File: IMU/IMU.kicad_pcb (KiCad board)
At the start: 2 copper layers, 14 parts, among them IC1 ADXL326BCPZ-RL7, U1 DEV-16771, U2 IAM-20380, U3 MLX90393SLW-ABA-011-RE

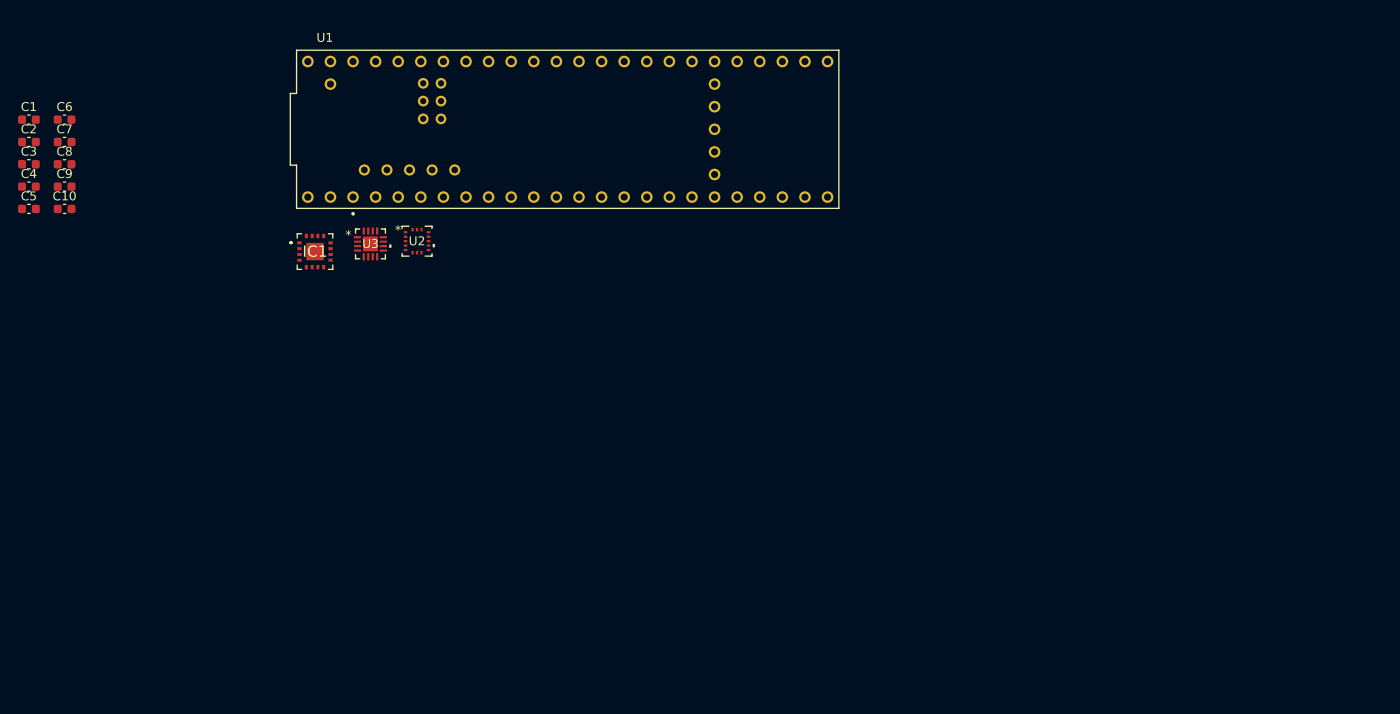
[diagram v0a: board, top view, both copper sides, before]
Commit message: Some layout changes
Added filled zomes, linked 3d models, added board edge cuts and mounting holes (still need to add filled zone exclusions around the mounting holes to prevent shorts, though I will probably just reduced the filled zomes anyways. Also should probably change which analog pins get used for the Gyro before routing traces/vias.
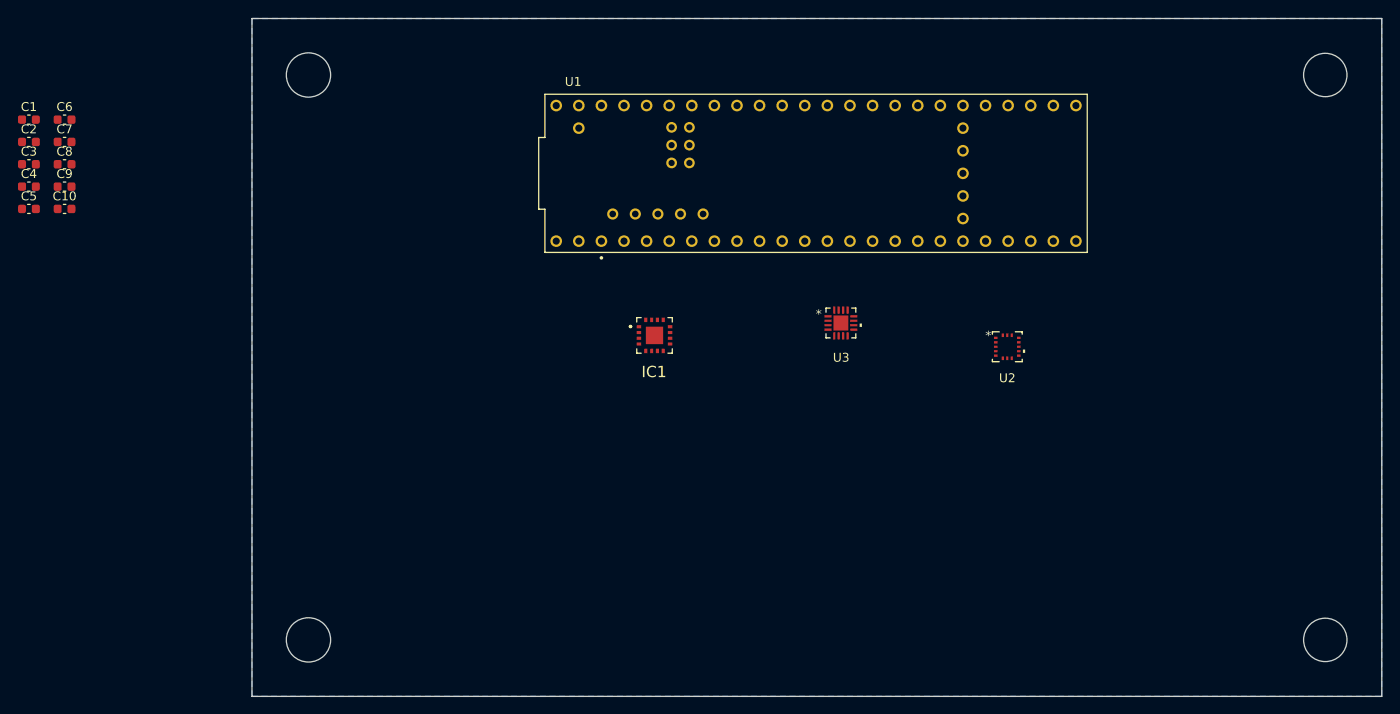
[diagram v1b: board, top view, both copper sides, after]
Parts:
- moved U2 67.4 mm to (172.0, 101.4)
- moved U3 53.6 mm to (153.3, 98.7)
- moved IC1 39.3 mm to (132.3, 100.1)
- moved U1 28.4 mm to (150.5, 81.9)
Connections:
- U1 pad GND1: unconnected-(U1-GND-PadGND1) -> /GND
- U1 pad GND2: unconnected-(U1-GND__1-PadGND2) -> /GND
- U1 pad GND3: unconnected-(U1-GND__2-PadGND3) -> /GND
- U1 pad GND4: unconnected-(U1-GND__3-PadGND4) -> /GND
- U1 pad GND5: unconnected-(U1-GND__4-PadGND5) -> /GND
- U1 pad USB_GND1: unconnected-(U1-USB_GND-PadUSB_GND1) -> /GND
- U1 pad USB_GND2: unconnected-(U1-USB_GND__1-PadUSB_GND2) -> /GND
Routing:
- added copper zone on In2.Cu, net /3P3V
- added copper zone on B.Cu, net /GND
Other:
- board outline added: 127 x 76.2 mm
- copper layers 2 -> 4

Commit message: Some minor Layout changes
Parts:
- added R1: 0, Resistor_SMD:R_0603_1608Metric, F.Cu at (143.0, 73.3)
- added R10: 0, Resistor_SMD:R_0603_1608Metric, F.Cu at (125.2, 100.5)
- added R11: 0, Resistor_SMD:R_0603_1608Metric, F.Cu at (145.5, 73.3)
- added R2: 0, Resistor_SMD:R_0603_1608Metric, F.Cu at (150.6, 100.8)
- added R3: 0, Resistor_SMD:R_0603_1608Metric, F.Cu at (155.6, 73.3)
- added R4: 0, Resistor_SMD:R_0603_1608Metric, F.Cu at (153.1, 100.8)
- added R5: 0, Resistor_SMD:R_0603_1608Metric, F.Cu at (155.7, 100.7)
- added R6: 0, Resistor_SMD:R_0603_1608Metric, F.Cu at (140.5, 73.3)
- added R7: 0, Resistor_SMD:R_0603_1608Metric, F.Cu at (168.5, 100.7)
- added R8: 0, Resistor_SMD:R_0603_1608Metric, F.Cu at (165.8, 100.7)
- added R9: 0, Resistor_SMD:R_0603_1608Metric, F.Cu at (127.8, 100.5)
- added TP1: TestPoint, TestPoint:TestPoint_Pad_4.0x4.0mm, F.Cu at (71.5, 107.7)
- added TP2: TestPoint, TestPoint:TestPoint_Pad_4.0x4.0mm, F.Cu at (71.5, 113.8)
- moved C5 75.9 mm to (133.2, 112.1)
- moved C6 72.3 mm to (130.3, 109.0)
- moved U2 35.7 mm to (136.8, 107.1)
- moved U3 19.6 mm to (171.4, 106.2)
- moved IC1 18.4 mm to (148.8, 108.2)
- moved U1 5.28 mm to (151.9, 87.0)
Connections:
- U2 pad 2: /SCK_Gyro -> Net-(U2-SCL/SPC)
- U2 pad 3: /MOSI_Gyro -> Net-(U2-SDA/SDI)
- U2 pad 4: /MISO_Gyro -> Net-(U2-SA0/SDO)
- U2 pad 5: /CS_Gyro -> Net-(U2-CS)
- U2 pad 6: /INT_Gyro -> Net-(U2-INT)
- U3 pad 1: /INT_Mag -> Net-(U3-INT)
- U3 pad 2: /CS_Mag -> Net-(U3-SENB/CS)
- U3 pad 3: /SCK_Mag -> Net-(U3-SCL/SCLK)
- U3 pad 5: /MOSI_Mag -> Net-(U3-SDA/MOSI)
- U3 pad 6: /MISO_Mag -> Net-(U3-MISO)
- U3 pad 7: /TRIG_Mag -> Net-(U3-INT/TRIG)

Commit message: m
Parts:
- removed C1, C2, C3: 3 nF, Capacitor_SMD:C_0603_1608Metric
- removed C4: 0.01 uF, Capacitor_SMD:C_0603_1608Metric
- removed IC1: ADXL326BCPZ-RL7, ADXL326BCPZ-RL7:ADXL326BCPZRL7
- removed R1, R10, R11, R2, R3, R4, R5, R6, R7, R8, R9: 0, Resistor_SMD:R_0603_1608Metric
- removed TP1, TP2: TestPoint, TestPoint:TestPoint_Pad_4.0x4.0mm
- removed U1: DEV-16771, DEV-16771:DEV-16771
- added U4: RASPBERRY_PI_PICO, Raspberry Pi:RASPBERRY_PI_PICO, F.Cu at (151.4, 81.0)
- added U5: ADXL380-1BCCZ-RL7, ADXL380:ADXL380, F.Cu at (132.8, 103.7)
- moved C8 108.6 mm to (169.2, 115.0)
- moved C7 108.5 mm to (169.2, 112.0)
- moved C10 71.3 mm to (132.6, 111.4)
- moved C9 71.3 mm to (132.6, 108.8)
- moved C6 38.9 mm to (169.2, 109.5)
- moved C5 35.8 mm to (166.3, 98.5)
- moved U2 32.2 mm to (168.8, 103.4), turned to 90 degrees
- moved U3 21.6 mm to (149.9, 103.8)
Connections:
- U2 pad 2: Net-(U2-SCL/SPC) -> /SCK_Gyro
- U2 pad 3: Net-(U2-SDA/SDI) -> /MOSI_Gyro
- U2 pad 4: Net-(U2-SA0/SDO) -> /MISO_Gyro
- U2 pad 5: Net-(U2-CS) -> /CS_Gyro
- U2 pad 6: Net-(U2-INT) -> /INT_Gyro
- U3 pad 1: Net-(U3-INT) -> /INT_Mag
- U3 pad 2: Net-(U3-SENB/CS) -> unconnected-(U3-SENB/CS-Pad2)
- U3 pad 3: Net-(U3-SCL/SCLK) -> /SCK_Mag
- U3 pad 5: Net-(U3-SDA/MOSI) -> /SDA_Mag
- U3 pad 6: Net-(U3-MISO) -> unconnected-(U3-MISO-Pad6)
- U3 pad 7: Net-(U3-INT/TRIG) -> unconnected-(U3-INT/TRIG-Pad7)
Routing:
- net /GND: track 0.00 -> 29.5 mm, vias 0 -> 9
- net /MISO_Gyro: track 0.00 -> 26.8 mm, vias 0 -> 1
- net /3P3V: track 0.00 -> 24.8 mm, vias 0 -> 9
- net /MOSI_Gyro: track 0.00 -> 21.6 mm, vias 0 -> 1
- net /SDA_Mag: track 0.00 -> 20.7 mm
- net /SCK_Gyro: track 0.00 -> 20.3 mm
- net /CS_Gyro: track 0.00 -> 18.1 mm
- net /ACCEL_SCLK: track 0.00 -> 17.4 mm
- net /ACCEL_CS: track 0.00 -> 17.0 mm, vias 0 -> 1
- net /SCK_Mag: track 0.00 -> 16.7 mm
- net /ACCEL_SDI: track 0.00 -> 16.4 mm, vias 0 -> 1
- net /ACCEL_SDO: track 0.00 -> 16.4 mm, vias 0 -> 1
- net /INT_Gyro: track 0.00 -> 15.9 mm, vias 0 -> 1
- net /INT_Mag: track 0.00 -> 15.5 mm
- net /ACCEL_INT: track 0.00 -> 13.3 mm
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
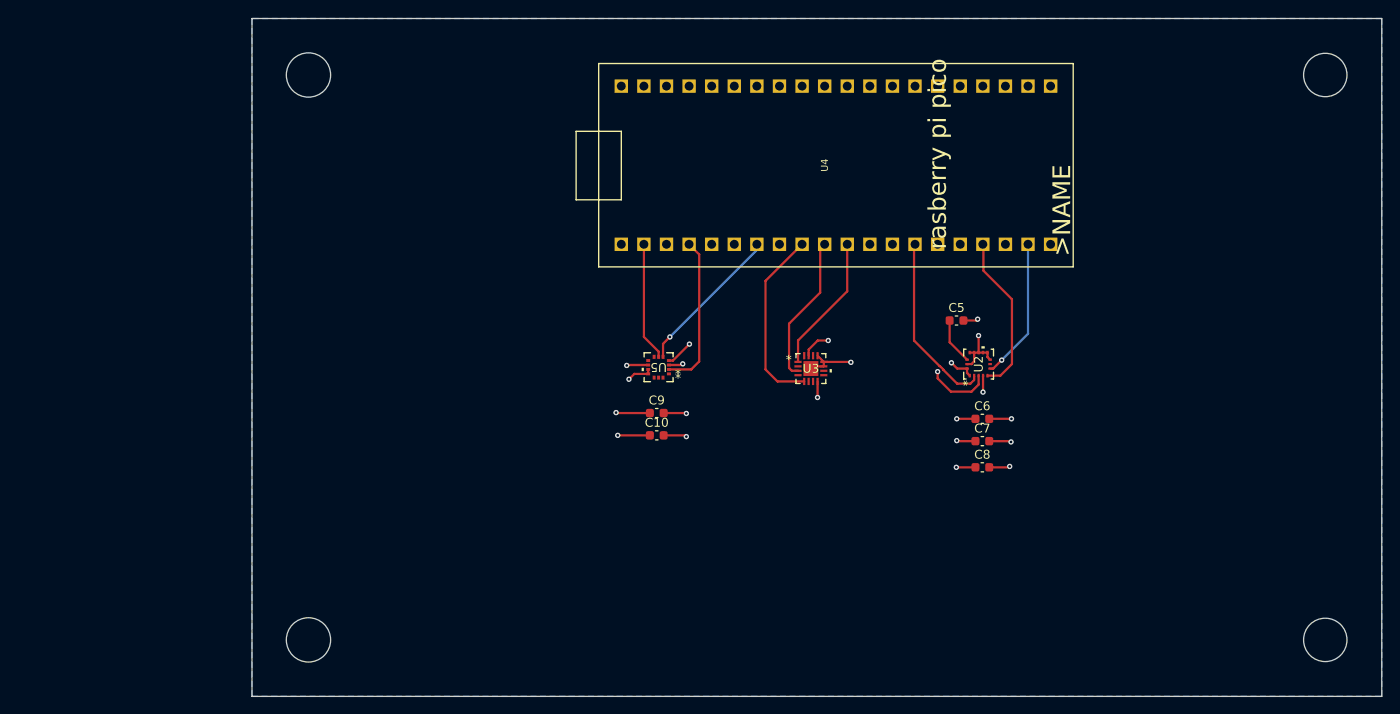
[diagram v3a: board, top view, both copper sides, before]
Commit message: fixed board size
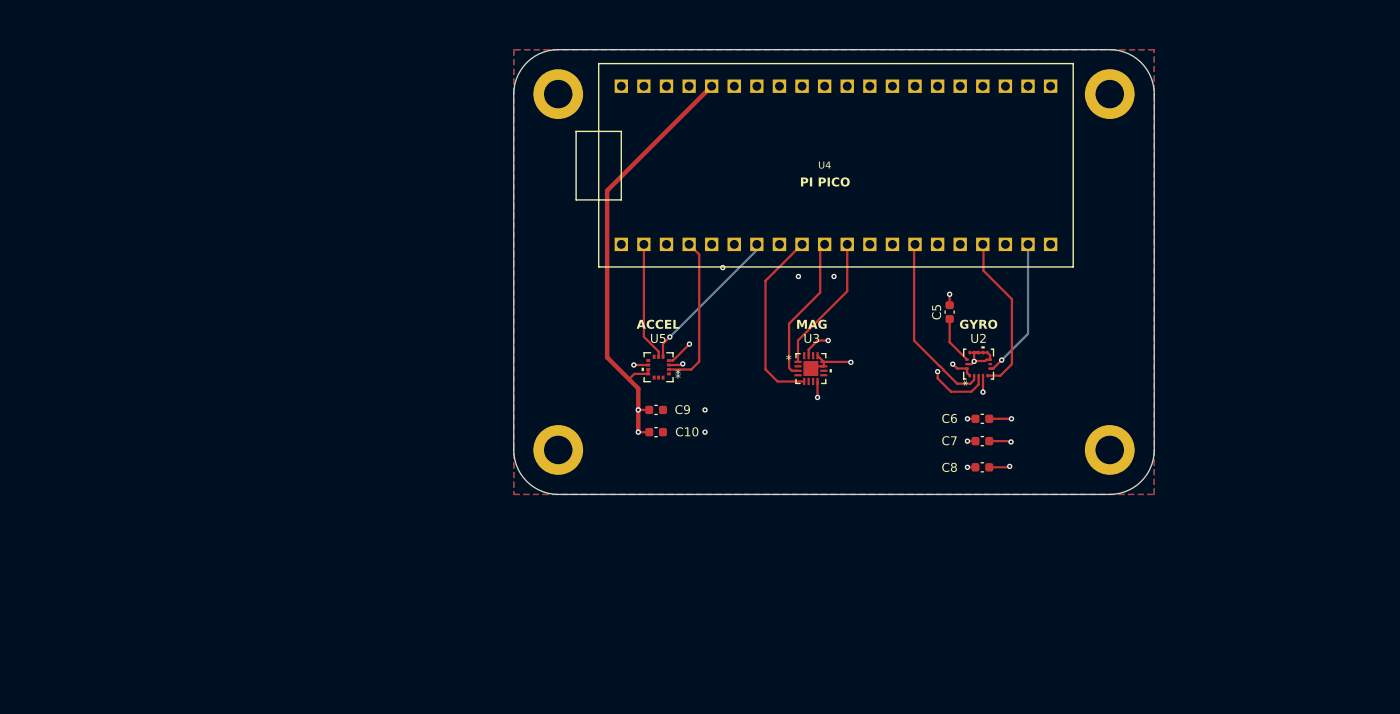
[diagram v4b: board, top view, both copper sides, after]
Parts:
- added H1: MountingHole_Pad, MountingHole:MountingHole_3.2mm_M3_DIN965_Pad, F.Cu at (121.5, 73.0)
- added H2: MountingHole_Pad, MountingHole:MountingHole_3.2mm_M3_DIN965_Pad, F.Cu at (183.5, 73.0)
- added H3: MountingHole_Pad, MountingHole:MountingHole_3.2mm_M3_DIN965_Pad, F.Cu at (121.5, 113.0)
- added H4: MountingHole_Pad, MountingHole:MountingHole_3.2mm_M3_DIN965_Pad, F.Cu at (183.5, 113.0)
- moved C5 1.23 mm to (165.5, 97.5), turned to 90 degrees
- moved C10 0.37 mm to (132.5, 111.0)
- moved C9 0.36 mm to (132.5, 108.5)
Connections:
- net /GND renamed GND
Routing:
- net /3P3V: track 24.8 -> 130.6 mm, vias 9 -> 8
- net GND: track 29.5 -> 23.6 mm, vias 9 -> 12
- added copper zone on F.Cu, net GND
- added copper zone on In1.Cu, net GND
- added copper zone on In2.Cu, net GND
- removed copper zone on In2.Cu, net /3P3V
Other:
- board size 127 x 76.2 mm -> 72 x 50 mm
- board text added: "ACCEL"
- board text added: "GYRO"
- board text added: "MAG"
- board text added: "PI PICO"

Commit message: fixed drc
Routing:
- net /3P3V: track 130.6 -> 128.7 mm, vias 8 -> 6
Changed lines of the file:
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@@
 	)
 	(segment
-		(start 130.5 108.5)
-		(end 130.5 106.1)
+		(start 127 83.86)
+		(end 127 102.6)
 		(width 0.5)
 		(layer "F.Cu")
@@
 	)
 	(segment
-		(start 130.5 108.5)
-		(end 130.5 111)
+		(start 138.75 72.11)
+		(end 127 83.86)
 		(width 0.5)
 		(layer "F.Cu")
@@
 		(end 130.05 104.45)
 		(width 0.254)
-		(layer "F.Cu")
-		(net 40)
-	)
-	(segment
-		(start 130.5 106.1)
-		(end 127 102.6)
-		(width 0.5)
 		(layer "F.Cu")
 		(net 40)
@@
 	)
 	(segment
-		(start 131.725 111)
-		(end 130.5 111)
-		(width 0.254)
-		(layer "F.Cu")
-		(net 40)
-	)
-	(segment
 		(start 167.5 112.01)
 		(end 168.4 112.01)
@@
 	)
 	(segment
-		(start 168.4 114.95)
-		(end 167.5 114.95)
-		(width 0.254)
+		(start 131.725 107.325)
+		(end 131.725 111)
+		(width 0.5)
 		(layer "F.Cu")
 		(net 40)
 	)
 	(segment
-		(start 127 102.6)
-		(end 127 83.86)
-		(width 0.5)
+		(start 168.4 114.95)
+		(end 167.5 114.95)
+		(width 0.254)
 		(layer "F.Cu")
 		(net 40)
@@
 	)
 	(segment
-		(start 149.6522 101.712799)
-		(end 150.664999 100.7)
-		(width 0.254)
+		(start 127 102.6)
+		(end 131.725 107.325)
+		(width 0.5)
 		(layer "F.Cu")
 		(net 40)
 	)
 	(segment
-		(start 130.5 108.5)
-		(end 131.725 108.5)
+		(start 149.6522 101.712799)
+		(end 150.664999 100.7)
 		(width 0.254)
 		(layer "F.Cu")
@@
 		(end 129.45 105.05)
 		(width 0.254)
-		(layer "F.Cu")
-		(net 40)
-	)
-	(segment
-		(start 127 83.86)
-		(end 138.75 72.11)
-		(width 0.5)
 		(layer "F.Cu")
 		(net 40)
@@
 	)
 	(via
-		(at 130.5 111)
-		(size 0.6)
-		(drill 0.3)
-		(layers "F.Cu" "B.Cu")
-		(net 40)
-	)
-	(via
 		(at 167.5 114.95)
 		(size 0.6)
 		(drill 0.3)
-		(layers "F.Cu" "B.Cu")
-		(net 40)
-	)
-	(via
-		(at 130.5 108.5)
-		(size 0.6)
-		(drill 0.3)

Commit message: Final Final Final Changes
Renamed accel SPI nets for clarity. Changed one of the internal planes to a power plane for 3P3V and removed 3P3V traces. Adjusted design constraints to eliminate DRC warnings/errors.
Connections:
- net /ACCEL_SDI renamed /ACCEL_MOSI
- net /ACCEL_SDO renamed /ACCEL_MISO
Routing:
- net /3P3V: track 128.7 -> 21.3 mm, vias 6 -> 9
- net GND: track 23.6 -> 16.1 mm, vias 12 -> 8
- added copper zone on In2.Cu, net /3P3V
- removed copper zone on In2.Cu, net GND
